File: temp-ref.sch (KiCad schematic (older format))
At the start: 42 parts, among them IC1 INA211AIDCKT, IC2 INA211AIDCKT, J1 Conn_01x05_Male, J2 USB_C_Receptacle_USB2.0, J3 Conn_02x04_Counter_Clockwise, Q1 Q_NMOS_GDS, Q2 MMBT3904, Q3 Q_NMOS_GDS, SW1 SW_SPST, SW2 SW_SPST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

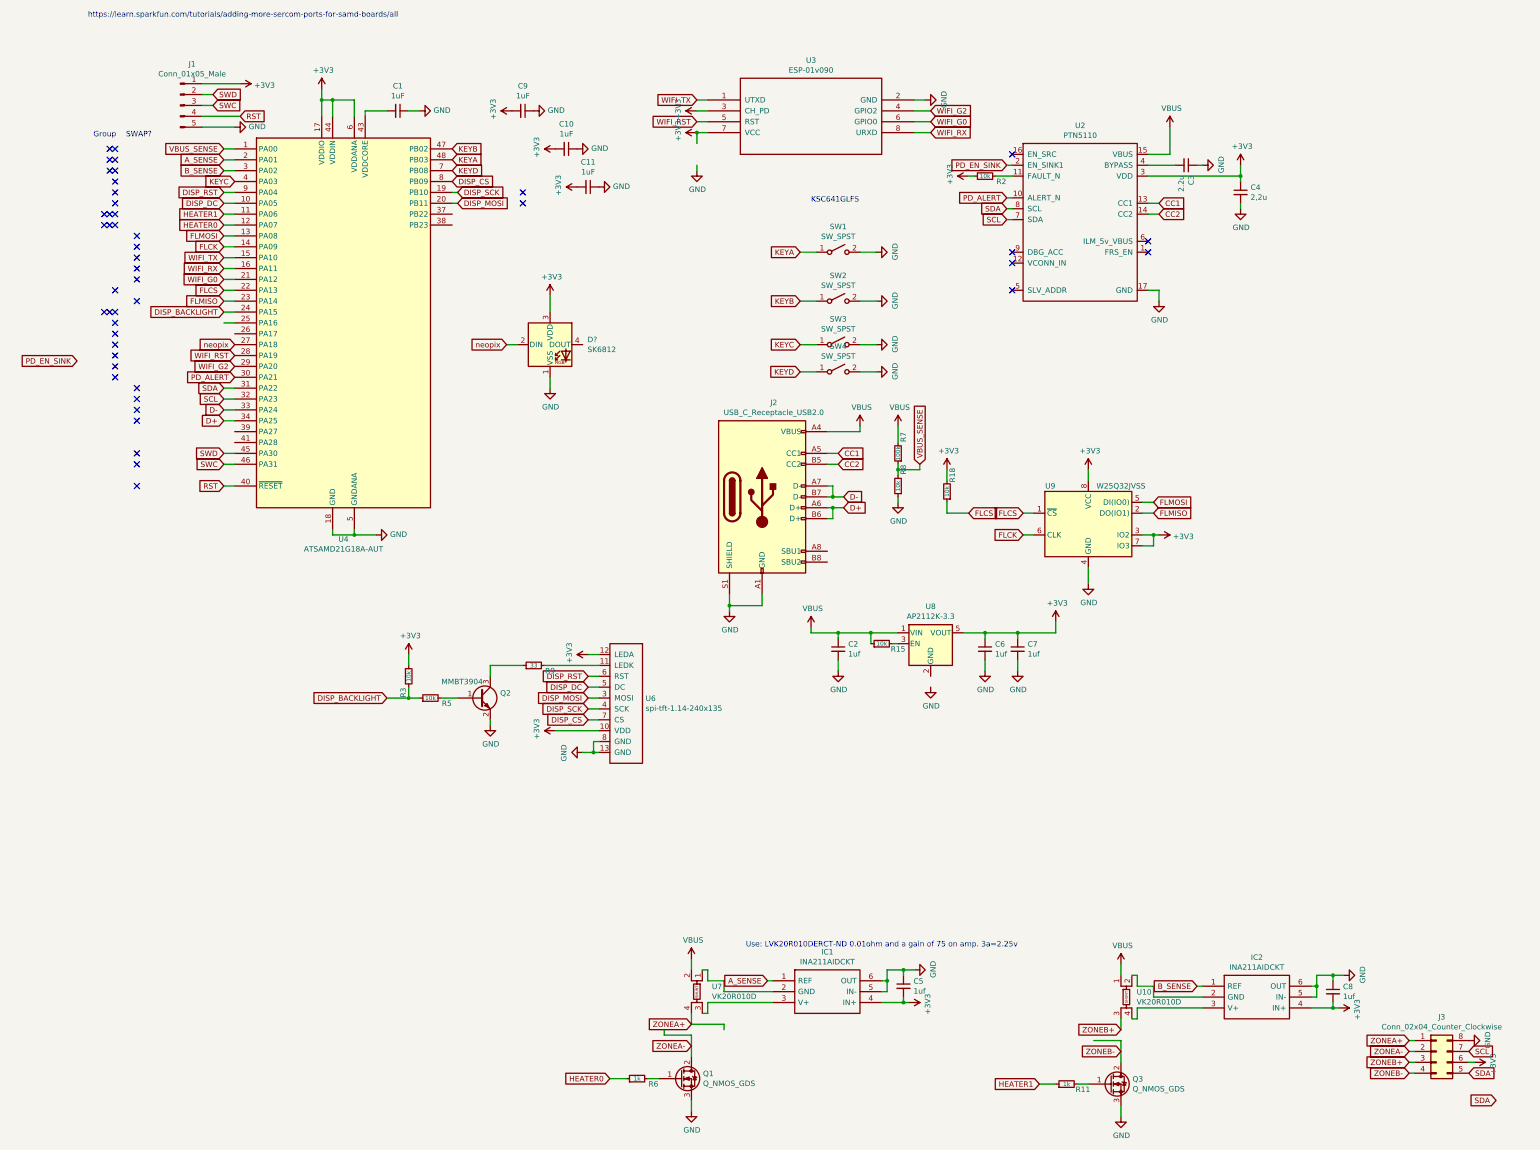
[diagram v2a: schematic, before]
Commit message: 3d models added, Added dallas pins, added nepixels, moved some elements around.
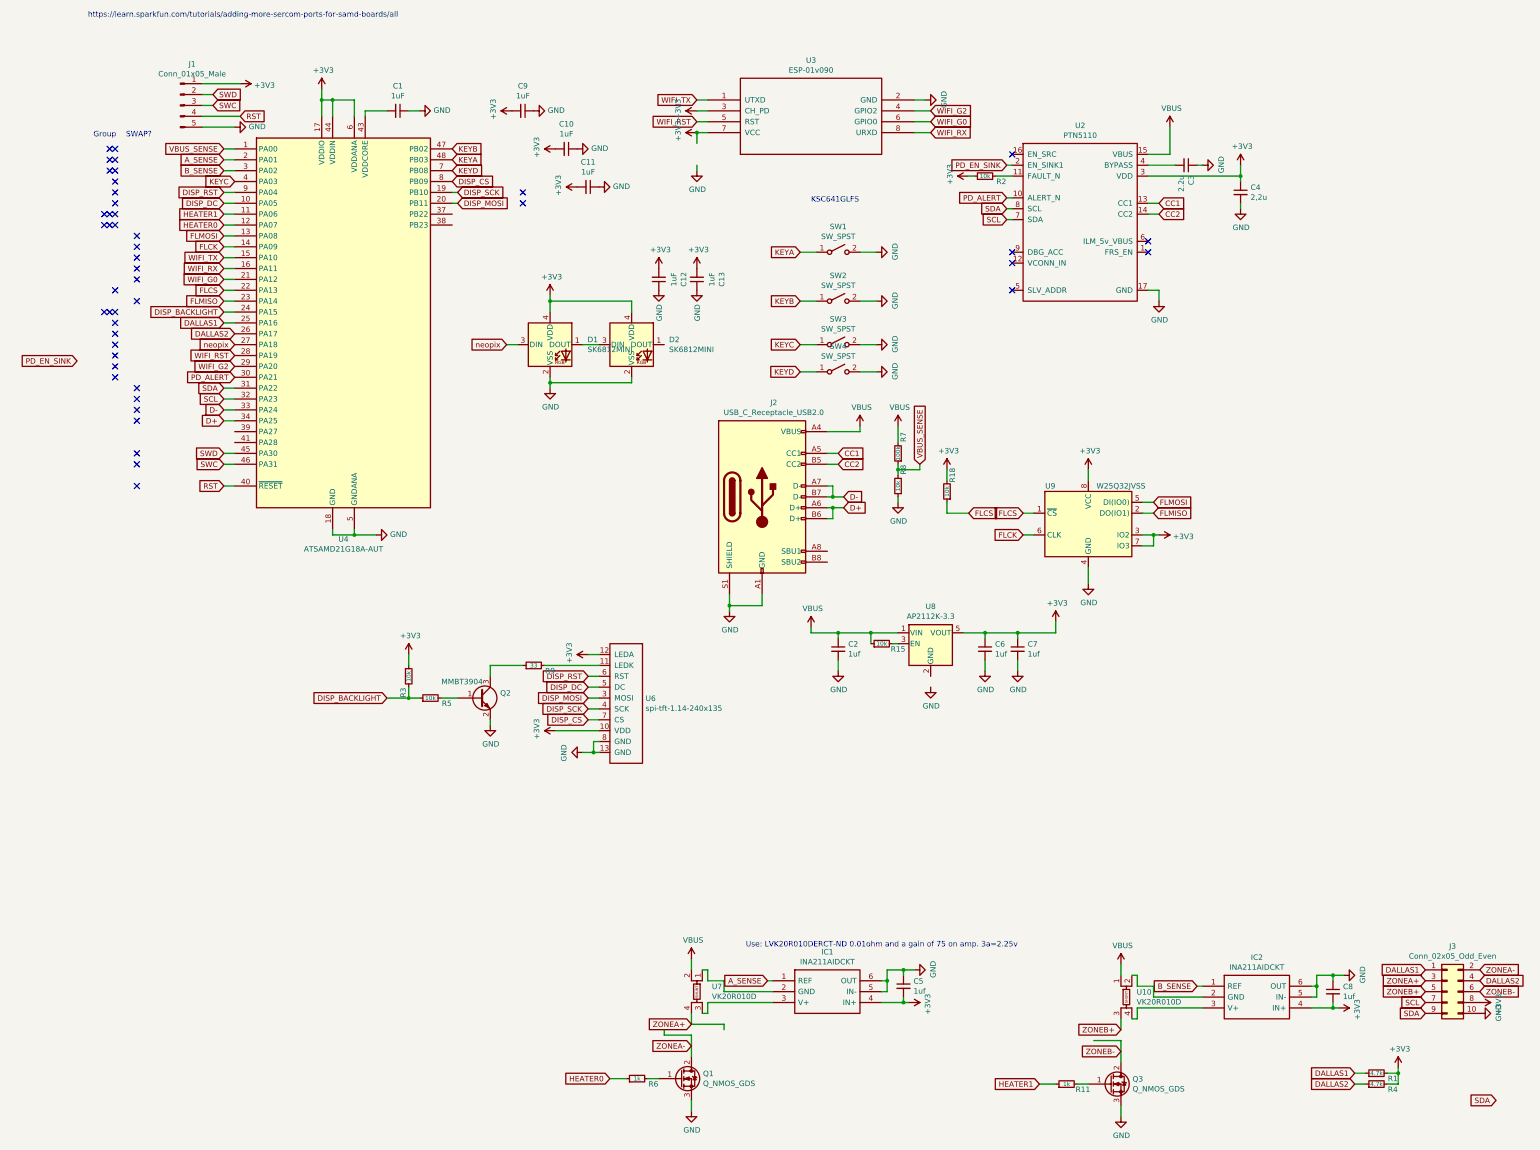
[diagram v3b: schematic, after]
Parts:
- removed D?: SK6812, LED_SMD:LED_SK6812_PLCC4_5.0x5.0mm_P3.2mm, symbol LED:SK6812
- removed J3: Conn_02x04_Counter_Clockwise, Connector_PinSocket_2.54mm:PinSocket_2x04_P2.54mm_Horizontal, symbol Connector_Generic:Conn_02x04_Counter_Clockwise
- added C12, C13: 1uF, Capacitor_SMD:C_0603_1608Metric, symbol Device:C_Small
- added D1, D2: SK6812MINI, temp-ref:LED_SK6812MINI_PLCC4_3.5x3.5mm_P1.75mm, symbol LED:SK6812MINI
- added J3: Conn_02x05_Odd_Even, Connector_PinSocket_2.54mm:PinSocket_2x05_P2.54mm_Horizontal, symbol Connector_Generic:Conn_02x05_Odd_Even
- added R1, R4: 4.7k, Resistor_SMD:R_0603_1608Metric, symbol Device:R_Small
- J2: footprint Connector_USB:USB_C_Receptacle_Amphenol_12401610E4-2A -> temp-ref:USB_C_Receptacle_Amphenol_12401610E4-2A
- U9: footprint Package_SO:SOIC-8_5.23x5.23mm_P1.27mm -> temp-ref:SOIC-8_5.23x5.23mm_P1.27mm
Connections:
- net +3V3: now also C12.2, C13.2, D1.4 (VDD), D2.4 (VDD), J3.8 (Pin_8), R1.2, R4.2
- net GND: now also C12.1, C13.1, D1.2 (VSS), D2.2 (VSS), J3.10 (Pin_10)
- net SCL: now also J3.7 (Pin_7)
- net SDA: now also J3.9 (Pin_9)
- net ZONEA+: now also J3.3 (Pin_3)
- net ZONEA-: now also J3.2 (Pin_2)
- net ZONEB+: now also J3.5 (Pin_5)
- net ZONEB-: now also J3.6 (Pin_6)
- net neopix: now also D1.3 (DIN)
- net DALLAS1: now reaches U4.25 (PA16)
- net DALLAS1: now also J3.1 (Pin_1), R1.1
- net DALLAS2: now reaches U4.26 (PA17)
- net DALLAS2: now also J3.4 (Pin_4), R4.1
- new net: D1.1 (DOUT), D2.3 (DIN)
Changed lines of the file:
@@
 F 0 "U9" H 9100 5100 50  0000 C CNN
 F 1 "W25Q32JVSS" H 9750 5100 50  0000 C CNN
-F 2 "Package_SO:SOIC-8_5.23x5.23mm_P1.27mm" H 9450 4750 50  0001 C CNN
+F 2 "temp-ref:SOIC-8_5.23x5.23mm_P1.27mm" H 9450 4750 50  0001 C CNN
 F 3 "http://www.winbond.com/resource-files/w25q32jv%20revg%2003272018%20plus.pdf" H 9450 4750 50  0001 C CNN
 	1    9450 4750
@@
 F 0 "J2" H 6557 5367 50  0000 C CNN
 F 1 "USB_C_Receptacle_USB2.0" H 6557 5276 50  0000 C CNN
-F 2 "Connector_USB:USB_C_Receptacle_Amphenol_12401610E4-2A" H 6600 4500 50  0001 C CNN
+F 2 "temp-ref:USB_C_Receptacle_Amphenol_12401610E4-2A" H 6600 4500 50  0001 C CNN
 F 3 "https://www.usb.org/sites/default/files/documents/usb_type-c.zip" H 6600 4500 50  0001 C CNN
 	1    6450 4500
@@
 Text GLabel 5800 9350 0    50   Input ~ 0
 ZONEA+
-Text GLabel 12400 9600 0    50   Input ~ 0
+Text GLabel 13050 8850 2    50   Input ~ 0
 ZONEA-
-Wire Wire Line
-	12450 9500 12400 9500
-Wire Wire Line
-	12450 9600 12400 9600
-Wire Wire Line
-	12450 9700 12400 9700
-Wire Wire Line
-	12450 9800 12400 9800
-Text GLabel 12400 9500 0    50   Input ~ 0
+Text GLabel 12550 8950 0    50   Input ~ 0
 ZONEA+
-Text GLabel 12400 9700 0    50   Input ~ 0
+Text GLabel 12550 9050 0    50   Input ~ 0
 ZONEB+
-Text GLabel 12400 9800 0    50   Input ~ 0
+Text GLabel 13050 9050 2    50   Input ~ 0
 ZONEB-
-$Comp
-L Connector_Generic:Conn_02x04_Counter_Clockwise J3
-U 1 1 5EDFE3CD
-P 12650 9600
-F 0 "J3" H 12700 9917 50  0000 C CNN
-F 1 "Conn_02x04_Counter_Clockwise" H 12700 9826 50  0000 C CNN
-F 2 "Connector_PinSocket_2.54mm:PinSocket_2x04_P2.54mm_Horizontal" H 12650 9600 50  0001 C CNN
-F 3 "~" H 12650 9600 50  0001 C CNN
-	1    12650 9600
-	1    0    0    -1
-$EndComp
-$Comp
-L power:GND #PWR0155
-U 1 1 5EE12D35
-P 12950 9500
-F 0 "#PWR0155" H 12950 9250 50  0001 C CNN
-F 1 "GND" H 12955 9327 50  0000 C CNN
-F 2 "" H 12950 9500 50  0001 C CNN
-F 3 "" H 12950 9500 50  0001 C CNN
-	1    12950 9500
-	0    -1   -1   0
-$EndComp
 $Comp
 L power:+3V3 #PWR0156
 U 1 1 5EE13BB6
-P 13000 9700
-F 0 "#PWR0156" H 13000 9550 50  0001 C CNN
-F 1 "+3V3" H 13015 9873 50  0000 C CNN
-F 2 "" H 13000 9700 50  0001 C CNN
-F 3 "" H 13000 9700 50  0001 C CNN
-	1    13000 9700
+P 13050 9150
+F 0 "#PWR0156" H 13050 9000 50  0001 C CNN
+F 1 "+3V3" H 13065 9323 50  0000 C CNN
+F 2 "" H 13050 9150 50  0001 C CNN
+F 3 "" H 13050 9150 50  0001 C CNN
+	1    13050 9150
 	0    1    1    0
 $EndComp
-Wire Wire Line
-	13000 9700 12950 9700
-Text GLabel 12950 9800 2    50   Input ~ 0
+Text GLabel 12550 9250 0    50   Input ~ 0
 SDA
 Text GLabel 13200 10050 0    50   Input ~ 0
 SDA
-Text GLabel 12950 9600 2    50   Input ~ 0
-SCL
 Wire Wire Line
 	1600 2900 1500 2900
@@
 $EndComp
 $Comp
-L LED:SK6812 D?
-U 1 1 5EB4B680
-P 4500 3100
-F 0 "D?" H 4844 3146 50  0000 L CNN
-F 1 "SK6812" H 4844 3055 50  0000 L CNN
-F 2 "LED_SMD:LED_SK6812_PLCC4_5.0x5.0mm_P3.2mm" H 4550 2800 50  0001 L TNN
-F 3 "https://cdn-shop.adafruit.com/product-files/1138/SK6812+LED+datasheet+.pdf" H 4600 2725 50  0001 L TNN
-	1    4500 3100
-	1    0    0    -1
-$EndComp
-$Comp
-L power:GND #PWR?
+L power:GND #PWR0141
 U 1 1 5EB4CC20
 P 4500 3500
-F 0 "#PWR?" H 4500 3250 50  0001 C CNN
+F 0 "#PWR0141" H 4500 3250 50  0001 C CNN
 F 1 "GND" H 4505 3327 50  0000 C CNN
 F 2 "" H 4500 3500 50  0001 C CNN
@@
 $EndComp
 $Comp
-L power:+3V3 #PWR?
+L power:+3V3 #PWR0142
 U 1 1 5EB4D1BE
 P 4500 2650
-F 0 "#PWR?" H 4500 2500 50  0001 C CNN
+F 0 "#PWR0142" H 4500 2500 50  0001 C CNN
 F 1 "+3V3" H 4515 2823 50  0000 C CNN
 F 2 "" H 4500 2650 50  0001 C CNN
@@
 $EndComp
 Wire Wire Line
-	4500 2650 4500 2800
-Wire Wire Line
-	4500 3400 4500 3500
+	4500 2650 4500 2700
 Text GLabel 4100 3100 0    50   Input ~ 0
 neopix
@@
 Text GLabel 1600 3100 0    50   Input ~ 0
 neopix
+$Comp
+L LED:SK6812MINI D1
+U 1 1 5EB8EF7F
+P 4500 3100
+F 0 "D1" H 4844 3146 50  0000 L CNN
+F 1 "SK6812MINI" H 4844 3055 50  0000 L CNN
+F 2 "temp-ref:LED_SK6812MINI_PLCC4_3.5x3.5mm_P1.75mm" H 4550 2800 50  0001 L TNN
+F 3 "https://cdn-shop.adafruit.com/product-files/2686/SK6812MINI_REV.01-1-2.pdf" H 4600 2725 50  0001 L TNN
+	1    4500 3100
+	1    0    0    -1
+$EndComp
+$Comp
+L LED:SK6812MINI D2
+U 1 1 5EB9A72A
+P 5250 3100
+F 0 "D2" H 5594 3146 50  0000 L CNN
+F 1 "SK6812MINI" H 5594 3055 50  0000 L CNN
+F 2 "temp-ref:LED_SK6812MINI_PLCC4_3.5x3.5mm_P1.75mm" H 5300 2800 50  0001 L TNN
+F 3 "https://cdn-shop.adafruit.com/product-files/2686/SK6812MINI_REV.01-1-2.pdf" H 5350 2725 50  0001 L TNN
+	1    5250 3100
+	1    0    0    -1
+$EndComp
+Wire Wire Line
+	4800 3100 4950 3100
+Wire Wire Line
+	4500 2700 5250 2700
+Wire Wire Line
+	5250 2700 5250 2800
+Connection ~ 4500 2700
+Wire Wire Line
+	4500 2700 4500 2800
+Wire Wire Line
+	5250 3400 5250 3450
+Wire Wire Line
+	5250 3450 4500 3450
+Wire Wire Line
+	4500 3400 4500 3450
+Connection ~ 4500 3450
+Wire Wire Line
+	4500 3450 4500 3500
+$Comp
+L Device:C_Small C12
+U 1 1 5EBCA9D7
+P 5500 2500
+F 0 "C12" V 5271 2500 50  0000 C CNN
+F 1 "1uF" V 5362 2500 50  0000 C CNN
+F 2 "Capacitor_SMD:C_0603_1608Metric" H 5500 2500 50  0001 C CNN
+F 3 "~" H 5500 2500 50  0001 C CNN
+	1    5500 2500
+	-1   0    0    1
+$EndComp
+$Comp
+L power:GND #PWR0157
+U 1 1 5EBCA9DD
+P 5500 2600
+F 0 "#PWR0157" H 5500 2350 50  0001 C CNN
+F 1 "GND" V 5505 2472 50  0000 R CNN
+F 2 "" H 5500 2600 50  0001 C CNN
+F 3 "" H 5500 2600 50  0001 C CNN
+	1    5500 2600
+	1    0    0    -1
+$EndComp
+$Comp
+L power:+3V3 #PWR0158
+U 1 1 5EBCA9E3
+P 5500 2400
+F 0 "#PWR0158" H 5500 2250 50  0001 C CNN
+F 1 "+3V3" H 5515 2573 50  0000 C CNN
+F 2 "" H 5500 2400 50  0001 C CNN
+F 3 "" H 5500 2400 50  0001 C CNN
+	1    5500 2400
+	1    0    0    -1
+$EndComp
+$Comp
+L Device:C_Small C13
+U 1 1 5EBD9D35
+P 5850 2500
+F 0 "C13" V 5621 2500 50  0000 C CNN
+F 1 "1uF" V 5712 2500 50  0000 C CNN
+F 2 "Capacitor_SMD:C_0603_1608Metric" H 5850 2500 50  0001 C CNN
+F 3 "~" H 5850 2500 50  0001 C CNN
+	1    5850 2500
+	-1   0    0    1
+$EndComp
+$Comp
+L power:GND #PWR0159
+U 1 1 5EBD9D3B
+P 5850 2600
+F 0 "#PWR0159" H 5850 2350 50  0001 C CNN
+F 1 "GND" V 5855 2472 50  0000 R CNN
+F 2 "" H 5850 2600 50  0001 C CNN
+F 3 "" H 5850 2600 50  0001 C CNN
+	1    5850 2600
+	1    0    0    -1
+$EndComp
+$Comp
+L power:+3V3 #PWR0160
+U 1 1 5EBD9D41
+P 5850 2400
+F 0 "#PWR0160" H 5850 2250 50  0001 C CNN
+F 1 "+3V3" H 5865 2573 50  0000 C CNN
+F 2 "" H 5850 2400 50  0001 C CNN
+F 3 "" H 5850 2400 50  0001 C CNN
+	1    5850 2400
+	1    0    0    -1
+$EndComp
+$Comp
+L power:GND #PWR0155
+U 1 1 5EE12D35
+P 13050 9250
+F 0 "#PWR0155" H 13050 9000 50  0001 C CNN
+F 1 "GND" H 13055 9077 50  0000 C CNN
+F 2 "" H 13050 9250 50  0001 C CNN
+F 3 "" H 13050 9250 50  0001 C CNN
+	1    13050 9250
+	0    -1   -1   0
+$EndComp
+Text GLabel 12550 9150 0    50   Input ~ 0
+SCL
+$Comp
+L Connector_Generic:Conn_02x05_Odd_Even J3
+U 1 1 5ECB2A06
+P 12750 9050
+F 0 "J3" H 12800 9467 50  0000 C CNN
+F 1 "Conn_02x05_Odd_Even" H 12800 9376 50  0000 C CNN
+F 2 "Connector_PinSocket_2.54mm:PinSocket_2x05_P2.54mm_Horizontal" H 12750 9050 50  0001 C CNN
+F 3 "~" H 12750 9050 50  0001 C CNN
+	1    12750 9050
+	1    0    0    -1
+$EndComp
+Text GLabel 1500 2900 0    50   Input ~ 0
+DALLAS1
+Text GLabel 1600 3000 0    50   Input ~ 0
+DALLAS2
+Text GLabel 12550 8850 0    50   Input ~ 0
+DALLAS1
+Text GLabel 11900 9900 0    50   Input ~ 0
+DALLAS2
+$Comp
+L Device:R_Small R1
+U 1 1 5ECE585D
+P 12100 9800
+F 0 "R1" V 12050 9650 50  0000 C CNN
+F 1 "4.7k" V 12100 9800 39  0000 C CNN
+F 2 "Resistor_SMD:R_0603_1608Metric" H 12100 9800 50  0001 C CNN
+F 3 "~" H 12100 9800 50  0001 C CNN
+	1    12100 9800
+	0    -1   -1   0
+$EndComp
+$Comp
+L Device:R_Small R4
+U 1 1 5ECE618D
+P 12100 9900
+F 0 "R4" V 12050 9750 50  0000 C CNN
+F 1 "4.7k" V 12100 9900 39  0000 C CNN
+F 2 "Resistor_SMD:R_0603_1608Metric" H 12100 9900 50  0001 C CNN
+F 3 "~" H 12100 9900 50  0001 C CNN
+	1    12100 9900
+	0    -1   -1   0
+$EndComp
+$Comp
+L power:+3V3 #PWR0161
+U 1 1 5ECE6399
+P 12300 9750
+F 0 "#PWR0161" H 12300 9600 50  0001 C CNN
+F 1 "+3V3" H 12315 9923 50  0000 C CNN
+F 2 "" H 12300 9750 50  0001 C CNN
+F 3 "" H 12300 9750 50  0001 C CNN
+	1    12300 9750
+	1    0    0    -1
+$EndComp
+Wire Wire Line
+	12200 9800 12300 9800
+Wire Wire Line
+	12300 9800 12300 9750
+Wire Wire Line
+	12200 9900 12300 9900
+Wire Wire Line
+	12300 9900 12300 9800
+Connection ~ 12300 9800
+Wire Wire Line
+	12000 9800 11900 9800
+Wire Wire Line
+	12000 9900 11900 9900
+Text GLabel 11900 9800 0    50   Input ~ 0
+DALLAS1
+Text GLabel 13050 8950 2    50   Input ~ 0
+DALLAS2
 $EndSCHEMATC

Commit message: fixes
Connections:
- net GND: now also U8.2 (GND)
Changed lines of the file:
@@
 Text GLabel 13050 8950 2    50   Input ~ 0
 DALLAS2
+Wire Wire Line
+	8000 6150 8000 6250
 $EndSCHEMATC
